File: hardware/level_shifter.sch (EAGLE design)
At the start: 14 parts, among them Q1 BS170, Q2 BS170

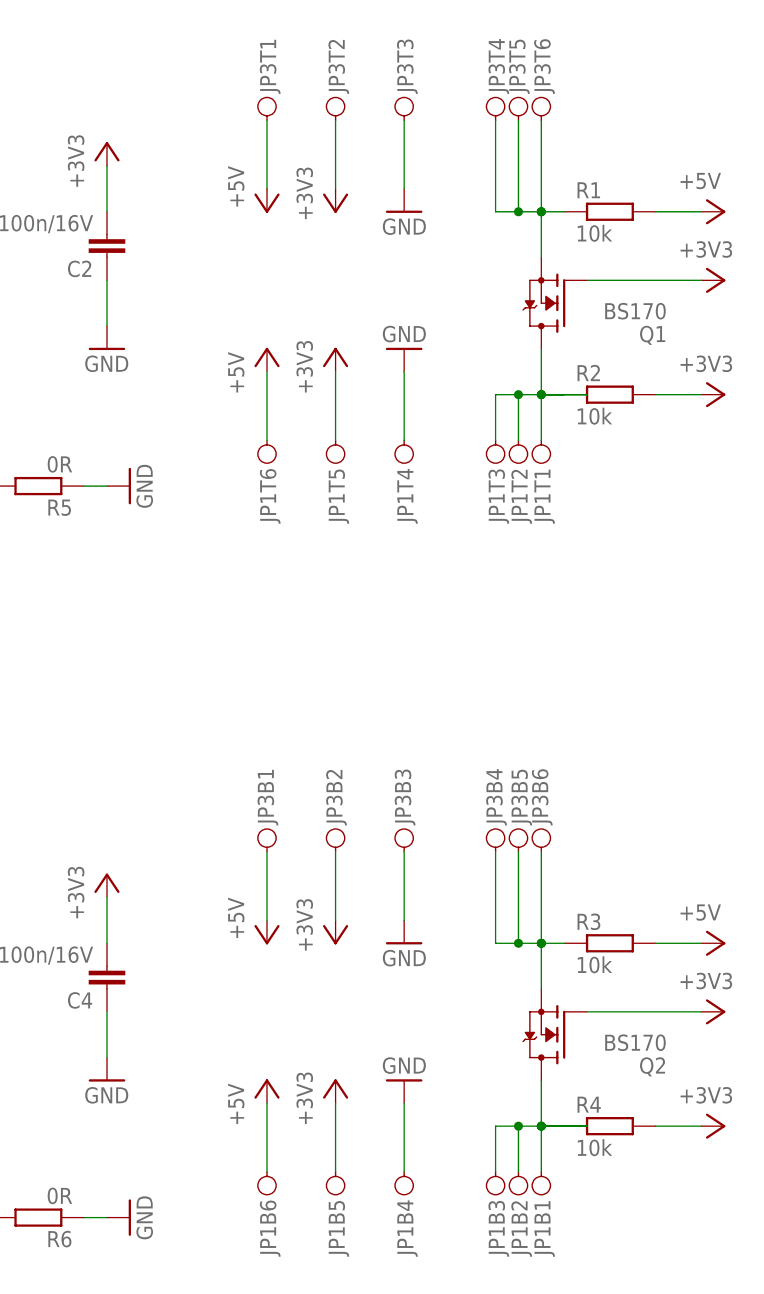
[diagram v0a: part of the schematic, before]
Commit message: shrunk level_shifter by one signal pinhead
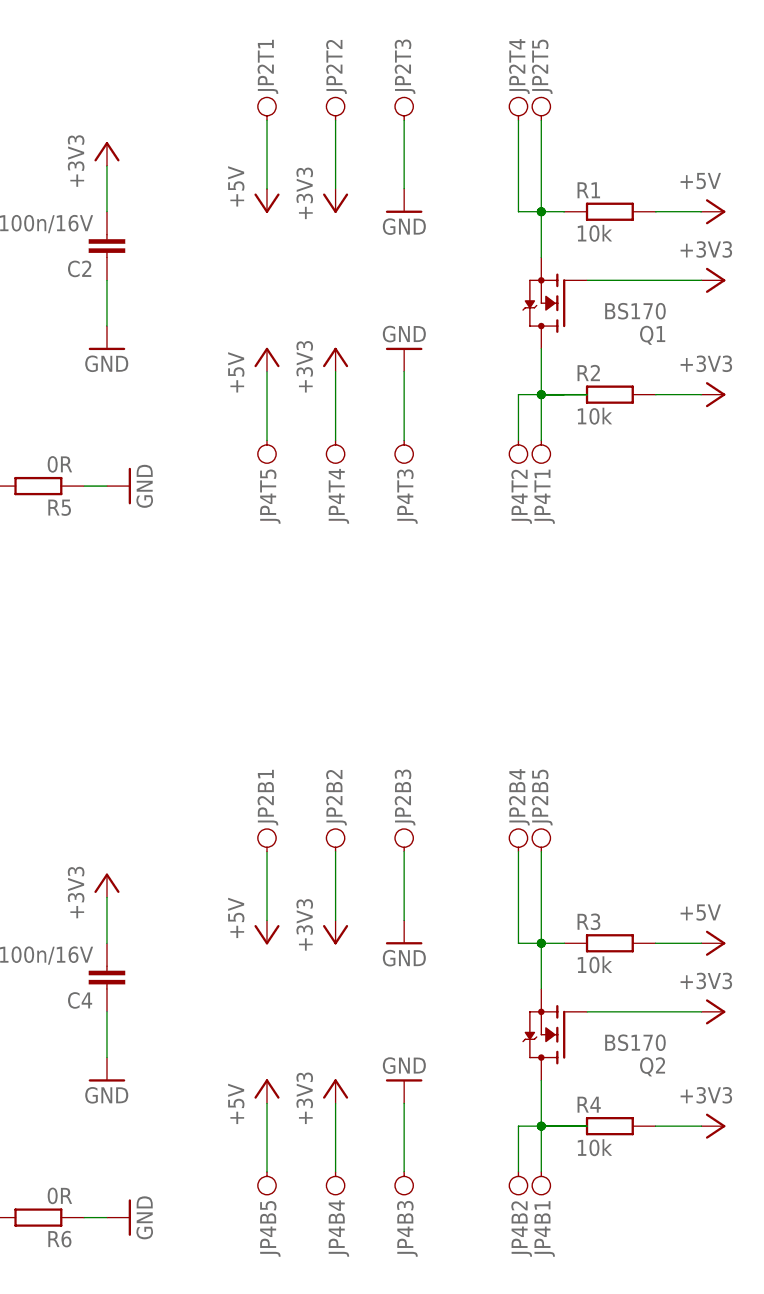
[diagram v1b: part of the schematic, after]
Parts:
- removed JP1, JP3: PINH2X06, pinhead_smd:PINH2X06
- added JP2, JP4: PINH2X05, pinhead_smd:PINH2X05
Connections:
- net +3V3: now also JP2B2.1, JP2T2.1, JP4B4.1, JP4T4.1; no longer JP1B5.1, JP1T5.1, JP3B2.1, JP3T2.1
- net +5V: now also JP2B1.1, JP2T1.1, JP4B5.1, JP4T5.1; no longer JP1B6.1, JP1T6.1, JP3B1.1, JP3T1.1
- net GND: now also JP2B3.1, JP2T3.1, JP4B3.1, JP4T3.1; no longer JP1B4.1, JP1T4.1, JP3B3.1, JP3T3.1
- net IN_B: now also JP4B1.1, JP4B2.1; no longer JP1B1.1, JP1B2.1, JP1B3.1
- net IN_T: now also JP4T1.1, JP4T2.1; no longer JP1T1.1, JP1T2.1, JP1T3.1
- net OUT_B: now also JP2B4.1, JP2B5.1; no longer JP3B4.1, JP3B5.1, JP3B6.1
- net OUT_T: now also JP2T4.1, JP2T5.1; no longer JP3T4.1, JP3T5.1, JP3T6.1

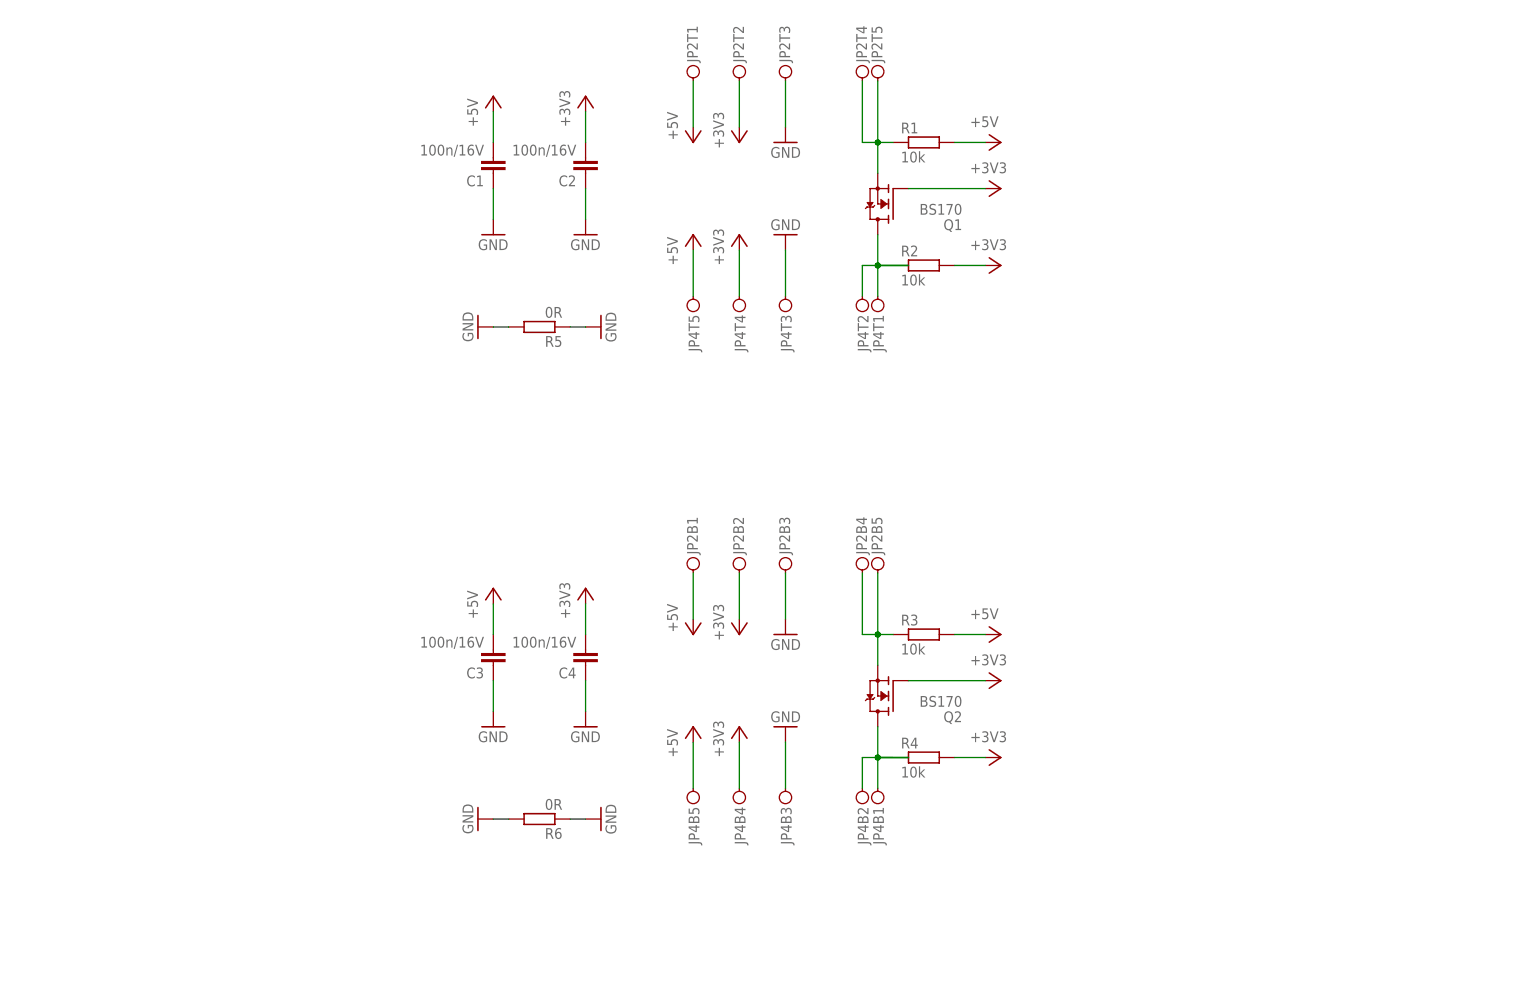
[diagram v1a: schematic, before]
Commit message: level_shifter: repair one polygon and add license to schema
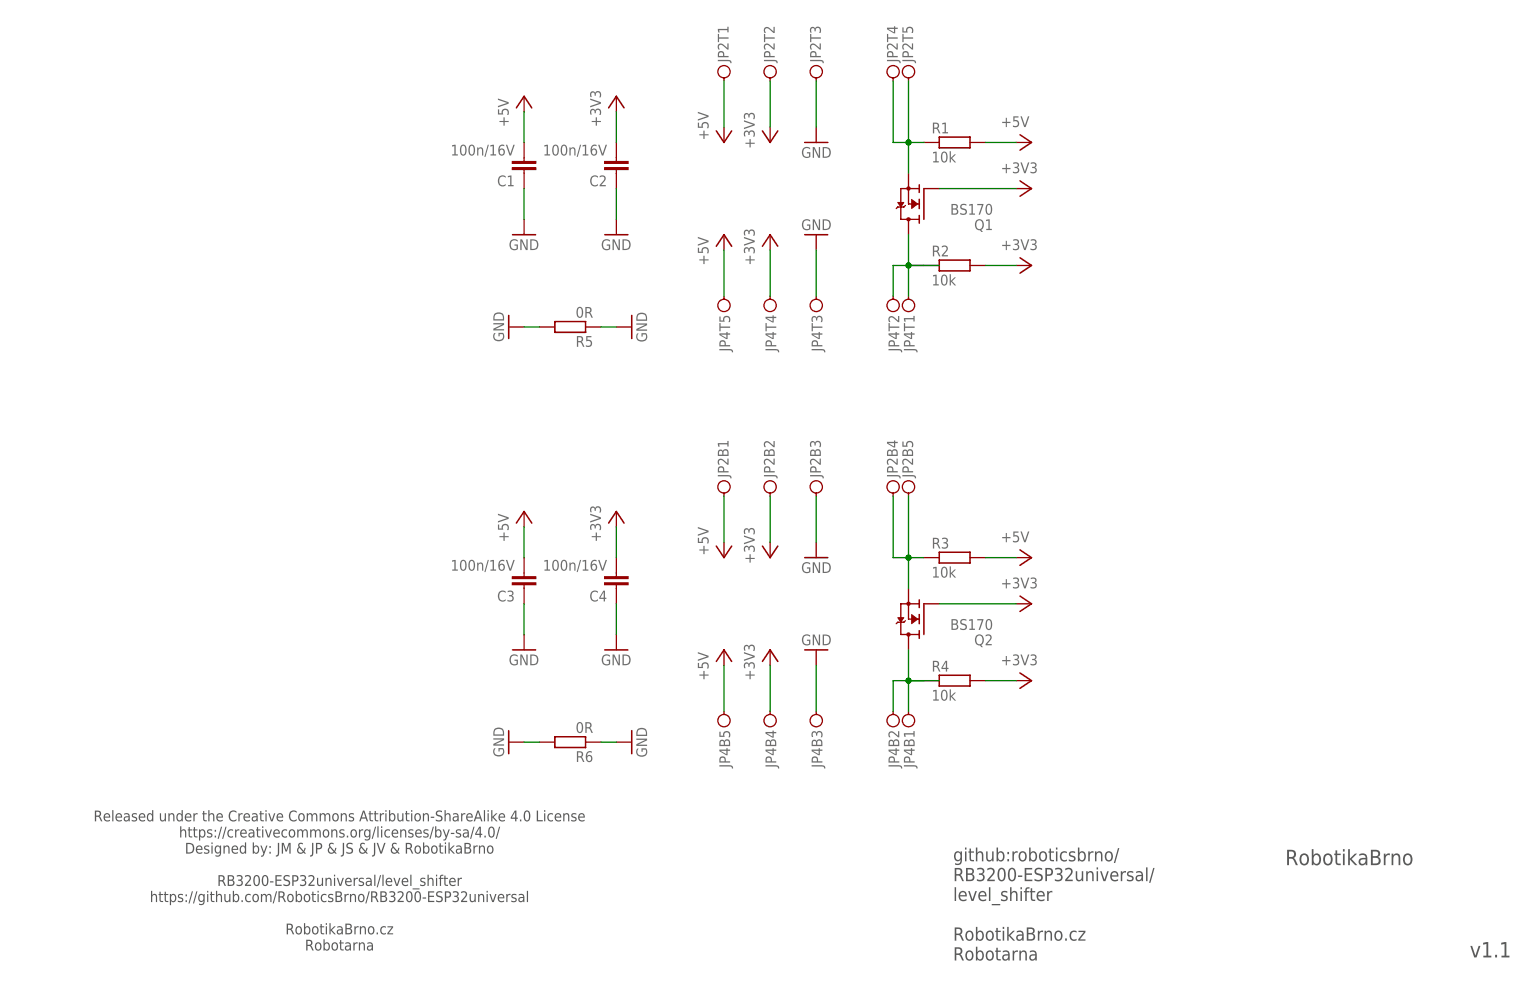
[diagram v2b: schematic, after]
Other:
- note added: "Released under the Creative Commons Attribution-ShareAlike 4.0 License https://creativecommons.org/licenses/by-sa/4.0/ Designed by: JM & JP & JS & JV & RobotikaBrno RB3200-ESP32universal/level_shifter https://github.com/RoboticsBrno/RB3200-ESP32universal RobotikaBrno.cz Robotarna"
- note added: "RobotikaBrno"
- note added: "github:roboticsbrno/ RB3200-ESP32universal/ level_shifter RobotikaBrno.cz Robotarna"
- note added: "v1.1"
- moved on the sheet: C1, C2, C3, C4, JP2B1, JP2B2, JP2B3, JP2B4, JP2B5, JP2T1, JP2T2, JP2T3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
